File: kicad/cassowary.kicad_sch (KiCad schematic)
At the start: 19 parts, among them U1 Pico

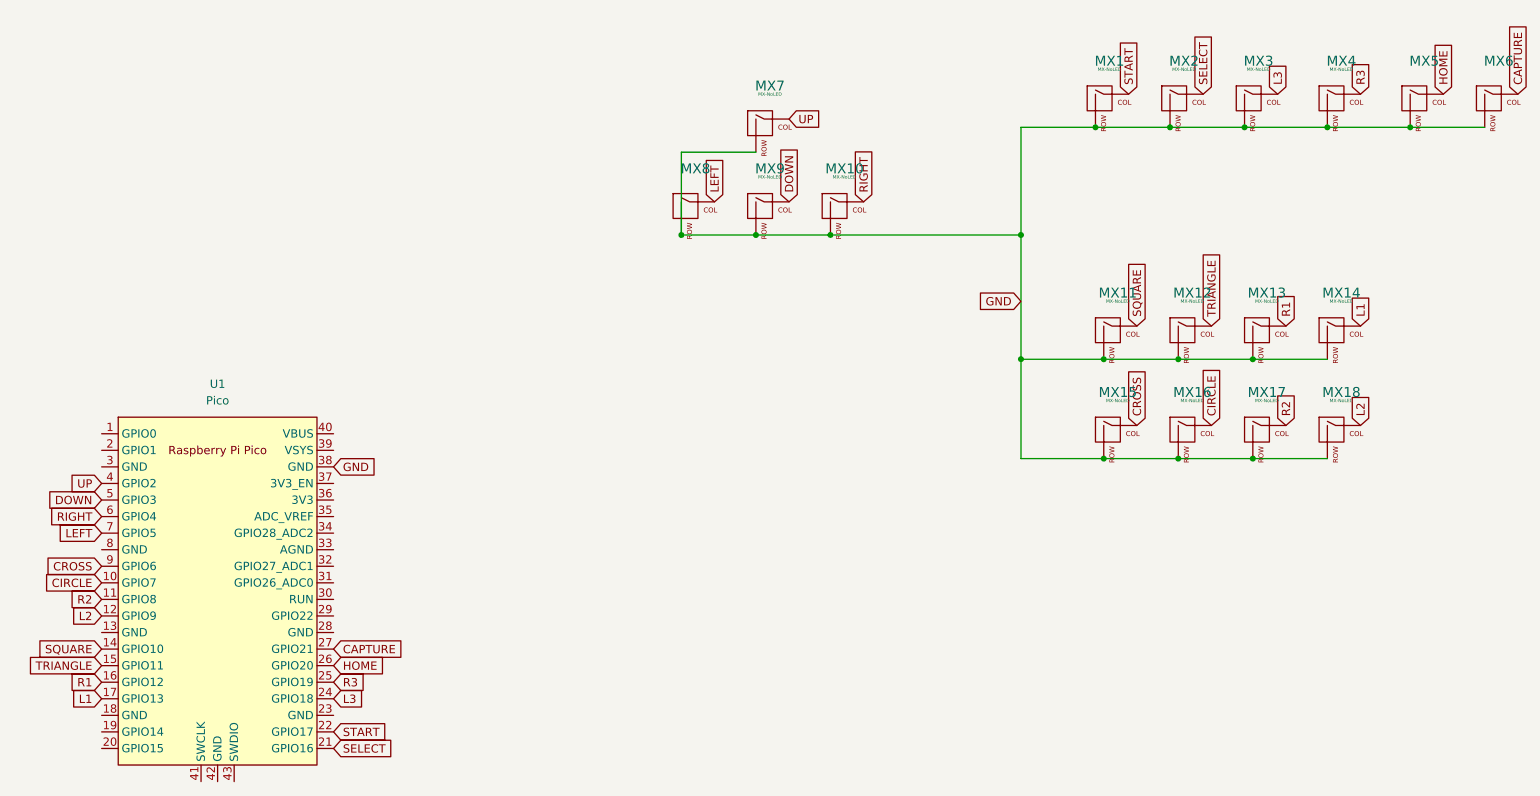
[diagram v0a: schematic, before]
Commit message: add thumb key and fill
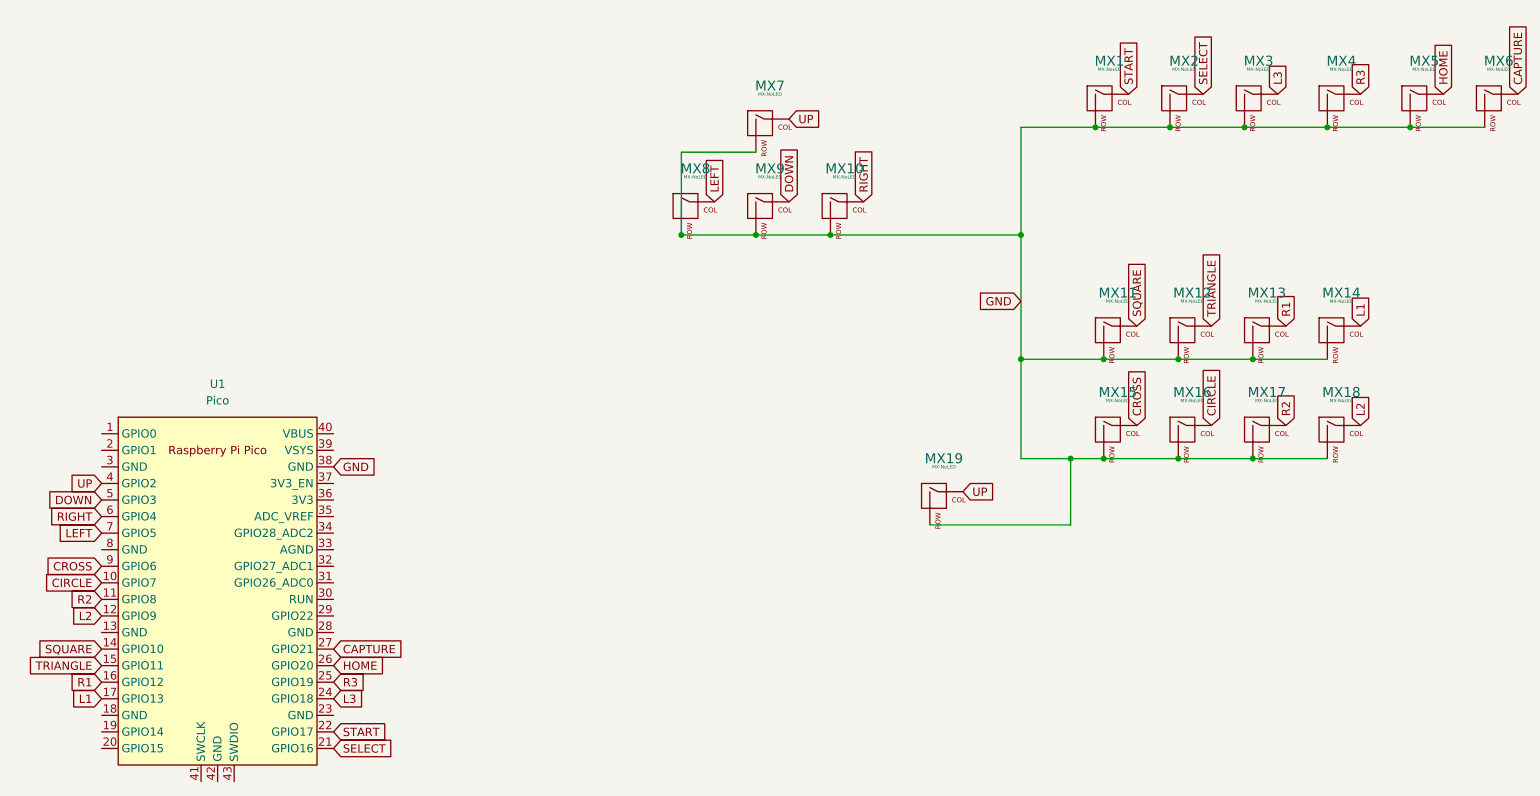
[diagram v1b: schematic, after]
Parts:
- added MX19: MX-NoLED, Switch_Keyboard_Cherry_MX:SW_Cherry_MX_PCB_1.00u, symbol MX_Alps_Hybrid:MX-NoLED
- MX1, MX10, MX11, MX12, MX13, MX14, MX15, MX16, MX17, MX18, MX2, MX3, MX4, MX7, MX9: footprint (none) -> Switch_Keyboard_Cherry_MX:SW_Cherry_MX_PCB_1.00u
- MX5, MX6, MX8: value (none) -> MX-NoLED; footprint (none) -> Switch_Keyboard_Cherry_MX:SW_Cherry_MX_PCB_1.00u
- U1: footprint (none) -> MCU_RaspberryPi_and_Boards:RPi_Pico_SMD_TH
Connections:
- net GND: now also MX19.2 (ROW)
- net UP: now also MX19.1 (COL)
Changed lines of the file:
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@@
   (junction (at 229.87 67.31) (diameter 0) (color 0 0 0 0)
   )
+  (junction (at 201.93 82.55) (diameter 0) (color 0 0 0 0)
+  )
   (junction (at 218.44 82.55) (diameter 0) (color 0 0 0 0)
   )
@@
     (stroke (width 0) (type default) (color 0 0 0 0))
   )
+  (wire (pts (xy 180.34 92.71) (xy 201.93 92.71))
+    (stroke (width 0) (type default) (color 0 0 0 0))
+  )
+  (wire (pts (xy 201.93 92.71) (xy 201.93 82.55))
+    (stroke (width 0) (type default) (color 0 0 0 0))
+  )
   (wire (pts (xy 217.17 31.75) (xy 228.6 31.75))
     (stroke (width 0) (type default) (color 0 0 0 0))
@@
     (stroke (width 0) (type default) (color 0 0 0 0))
   )
-  (wire (pts (xy 207.01 82.55) (xy 194.31 82.55))
+  (wire (pts (xy 207.01 82.55) (xy 201.93 82.55))
     (stroke (width 0) (type default) (color 0 0 0 0))
   )
@@
     (stroke (width 0) (type default) (color 0 0 0 0))
   )
+  (wire (pts (xy 201.93 82.55) (xy 194.31 82.55))
+    (stroke (width 0) (type default) (color 0 0 0 0))
+  )
   (wire (pts (xy 241.3 31.75) (xy 254 31.75))
     (stroke (width 0) (type default) (color 0 0 0 0))
@@
     )
   )
+  (global_label "UP" (shape input) (at 185.42 87.63 0) (fields_autoplaced)
+    (effects (font (size 1.27 1.27)) (justify left))
+    (property "Intersheet References" "${INTERSHEET_REFS}" (id 0) (at 190.4336 87.5506 0)
+      (effects (font (size 1.27 1.27)) (justify left) hide)
+    )
+  )
   (global_label "L2" (shape input) (at 246.38 77.47 90) (fields_autoplaced)
     (effects (font (size 1.27 1.27)) (justify left))
@@
       (effects (font (size 0.508 0.508)))
     )
-    (property "Footprint" "" (id 2) (at 139.065 45.085 0)
+    (property "Footprint" "Switch_Keyboard_Cherry_MX:SW_Cherry_MX_PCB_1.00u" (id 2) (at 139.065 45.085 0)
       (effects (font (size 1.524 1.524)) hide)
     )
@@
       (effects (font (size 0.508 0.508)))
     )
-    (property "Footprint" "" (id 2) (at 150.495 45.085 0)
+    (property "Footprint" "Switch_Keyboard_Cherry_MX:SW_Cherry_MX_PCB_1.00u" (id 2) (at 150.495 45.085 0)
       (effects (font (size 1.524 1.524)) hide)
     )
@@
       (effects (font (size 0.508 0.508)))
     )
-    (property "Footprint" "" (id 2) (at 203.835 64.135 0)
+    (property "Footprint" "Switch_Keyboard_Cherry_MX:SW_Cherry_MX_PCB_1.00u" (id 2) (at 203.835 64.135 0)
       (effects (font (size 1.524 1.524)) hide)
     )
@@
       (effects (font (size 1.524 1.524)))
     )
-    (property "Value" "" (id 1) (at 256.1556 22.86 0)
-      (effects (font (size 0.508 0.508)))
-    )
-    (property "Footprint" "" (id 2) (at 239.395 28.575 0)
+    (property "Value" "MX-NoLED" (id 1) (at 256.1556 22.86 0)
+      (effects (font (size 0.508 0.508)))
+    )
+    (property "Footprint" "Switch_Keyboard_Cherry_MX:SW_Cherry_MX_PCB_1.00u" (id 2) (at 239.395 28.575 0)
       (effects (font (size 1.524 1.524)) hide)
     )
@@
       (effects (font (size 0.508 0.508)))
     )
-    (property "Footprint" "" (id 2) (at 215.265 64.135 0)
+    (property "Footprint" "Switch_Keyboard_Cherry_MX:SW_Cherry_MX_PCB_1.00u" (id 2) (at 215.265 64.135 0)
       (effects (font (size 1.524 1.524)) hide)
     )
@@
       (effects (font (size 0.508 0.508)))
     )
-    (property "Footprint" "" (id 2) (at 226.695 79.375 0)
+    (property "Footprint" "Switch_Keyboard_Cherry_MX:SW_Cherry_MX_PCB_1.00u" (id 2) (at 226.695 79.375 0)
       (effects (font (size 1.524 1.524)) hide)
     )
@@
       (effects (font (size 1.524 1.524)))
     )
-    (property "Value" "" (id 1) (at 144.3956 39.37 0)
-      (effects (font (size 0.508 0.508)))
-    )
-    (property "Footprint" "" (id 2) (at 127.635 45.085 0)
+    (property "Value" "MX-NoLED" (id 1) (at 144.3956 39.37 0)
+      (effects (font (size 0.508 0.508)))
+    )
+    (property "Footprint" "Switch_Keyboard_Cherry_MX:SW_Cherry_MX_PCB_1.00u" (id 2) (at 127.635 45.085 0)
       (effects (font (size 1.524 1.524)) hide)
     )
@@
       (effects (font (size 0.508 0.508)))
     )
-    (property "Footprint" "" (id 2) (at 226.695 28.575 0)
+    (property "Footprint" "Switch_Keyboard_Cherry_MX:SW_Cherry_MX_PCB_1.00u" (id 2) (at 226.695 28.575 0)
       (effects (font (size 1.524 1.524)) hide)
     )
@@
     (property "Reference" "U1" (id 0) (at 71.12 71.12 0))
     (property "Value" "Pico" (id 1) (at 71.12 73.66 0))
-    (property "Footprint" "" (id 2) (at 71.12 102.87 90)
+    (property "Footprint" "MCU_RaspberryPi_and_Boards:RPi_Pico_SMD_TH" (id 2) (at 71.12 102.87 90)
       (effects (font (size 1.27 1.27)) hide)
     )
@@
       (effects (font (size 0.508 0.508)))
     )
-    (property "Footprint" "" (id 2) (at 192.405 64.135 0)
+    (property "Footprint" "Switch_Keyboard_Cherry_MX:SW_Cherry_MX_PCB_1.00u" (id 2) (at 192.405 64.135 0)
       (effects (font (size 1.524 1.524)) hide)
     )
@@
       (effects (font (size 0.508 0.508)))
     )
-    (property "Footprint" "" (id 2) (at 213.995 28.575 0)
+    (property "Footprint" "Switch_Keyboard_Cherry_MX:SW_Cherry_MX_PCB_1.00u" (id 2) (at 213.995 28.575 0)
       (effects (font (size 1.524 1.524)) hide)
     )
@@
       (effects (font (size 0.508 0.508)))
     )
-    (property "Footprint" "" (id 2) (at 203.835 79.375 0)
+    (property "Footprint" "Switch_Keyboard_Cherry_MX:SW_Cherry_MX_PCB_1.00u" (id 2) (at 203.835 79.375 0)
       (effects (font (size 1.524 1.524)) hide)
     )
@@
       (effects (font (size 0.508 0.508)))
     )
-    (property "Footprint" "" (id 2) (at 192.405 79.375 0)
+    (property "Footprint" "Switch_Keyboard_Cherry_MX:SW_Cherry_MX_PCB_1.00u" (id 2) (at 192.405 79.375 0)
       (effects (font (size 1.524 1.524)) hide)
     )
@@
       (effects (font (size 0.508 0.508)))
     )
-    (property "Footprint" "" (id 2) (at 226.695 64.135 0)
+    (property "Footprint" "Switch_Keyboard_Cherry_MX:SW_Cherry_MX_PCB_1.00u" (id 2) (at 226.695 64.135 0)
       (effects (font (size 1.524 1.524)) hide)
     )
@@
       (effects (font (size 0.508 0.508)))
     )
-    (property "Footprint" "" (id 2) (at 202.565 28.575 0)
+    (property "Footprint" "Switch_Keyboard_Cherry_MX:SW_Cherry_MX_PCB_1.00u" (id 2) (at 202.565 28.575 0)
       (effects (font (size 1.524 1.524)) hide)
     )
@@
       (effects (font (size 1.524 1.524)))
     )
-    (property "Value" "" (id 1) (at 267.5856 22.86 0)
-      (effects (font (size 0.508 0.508)))
-    )
-    (property "Footprint" "" (id 2) (at 250.825 28.575 0)
+    (property "Value" "MX-NoLED" (id 1) (at 267.5856 22.86 0)
+      (effects (font (size 0.508 0.508)))
+    )
+    (property "Footprint" "Switch_Keyboard_Cherry_MX:SW_Cherry_MX_PCB_1.00u" (id 2) (at 250.825 28.575 0)
       (effects (font (size 1.524 1.524)) hide)
     )
@@
       (effects (font (size 0.508 0.508)))
     )
-    (property "Footprint" "" (id 2) (at 191.135 28.575 0)
+    (property "Footprint" "Switch_Keyboard_Cherry_MX:SW_Cherry_MX_PCB_1.00u" (id 2) (at 191.135 28.575 0)
       (effects (font (size 1.524 1.524)) hide)
     )
@@
       (effects (font (size 0.508 0.508)))
     )
-    (property "Footprint" "" (id 2) (at 215.265 79.375 0)
+    (property "Footprint" "Switch_Keyboard_Cherry_MX:SW_Cherry_MX_PCB_1.00u" (id 2) (at 215.265 79.375 0)
       (effects (font (size 1.524 1.524)) hide)
     )
@@
       (effects (font (size 0.508 0.508)))
     )
-    (property "Footprint" "" (id 2) (at 139.065 32.385 0)
+    (property "Footprint" "Switch_Keyboard_Cherry_MX:SW_Cherry_MX_PCB_1.00u" (id 2) (at 139.065 32.385 0)
       (effects (font (size 1.524 1.524)) hide)
     )
     (property "Datasheet" "" (id 3) (at 139.065 32.385 0)
+      (effects (font (size 1.524 1.524)) hide)
+    )
+    (pin "1")
+    (pin "2")
+  )
+  (symbol (lib_id "MX_Alps_Hybrid:MX-NoLED") (at 181.61 88.9 0) (unit 1)
+    (in_bom yes) (on_board yes) (fields_autoplaced)
+    (property "Reference" "MX19" (id 0) (at 182.4956 82.55 0)
+      (effects (font (size 1.524 1.524)))
+    )
+    (property "Value" "MX-NoLED" (id 1) (at 182.4956 83.82 0)
+      (effects (font (size 0.508 0.508)))
+    )
+    (property "Footprint" "Switch_Keyboard_Cherry_MX:SW_Cherry_MX_PCB_1.00u" (id 2) (at 165.735 89.535 0)
+      (effects (font (size 1.524 1.524)) hide)
+    )
+    (property "Datasheet" "" (id 3) (at 165.735 89.535 0)
       (effects (font (size 1.524 1.524)) hide)
     )
@@
       (reference "MX18") (unit 1) (value "MX-NoLED") (footprint "Switch_Keyboard_Cherry_MX:SW_Cherry_MX_PCB_1.00u")
     )
+    (path "/ea41d734-15a4-4b77-8914-ba79d2370ec5"
+      (reference "MX19") (unit 1) (value "MX-NoLED") (footprint "Switch_Keyboard_Cherry_MX:SW_Cherry_MX_PCB_1.00u")
+    )
     (path "/578783be-47eb-4de7-bfa7-4193fd4bc187"
